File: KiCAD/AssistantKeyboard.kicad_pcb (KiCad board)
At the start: 2 copper layers, 64 x 108 mm, 14 parts, among them J1 Conn_01x04_Male, J2 Conn_01x12_Male, J3 Conn_01x12_Male, J4 Conn_01x02_Male, SW1 SW_Push, SW13 RotaryEncoder_Switch, SW2 SW_Push, SW3 SW_Push, SW4 SW_Push, SW5 SW_Push, SW6 SW_Push, SW7 SW_Push, SW8 SW_Push, SW9 SW_Push

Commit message: V1.0
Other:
- board text added: "AssistantKeyboard by A. Hensel v.1.0"
- board text removed: "AssistantKeyboard by A. Hensel v.0.9"
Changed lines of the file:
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@@
     (effects (font (size 1.5 1.5) (thickness 0.3)))
   )
-  (gr_text "AssistantKeyboard\nby A. Hensel\nv.0.9" (at 111.252 49.53) (layer "F.SilkS")
-    (effects (font (size 1 1) (thickness 0.15)))
+  (gr_text "AssistantKeyboard\nby A. Hensel\nv.1.0" (at 111.252 49.53) (layer "F.SilkS")
+    (effects (font (size 1.2 1.2) (thickness 0.15)))
   )
   (gr_text "Display I²C" (at 115.57 66.802 90) (layer "F.SilkS")

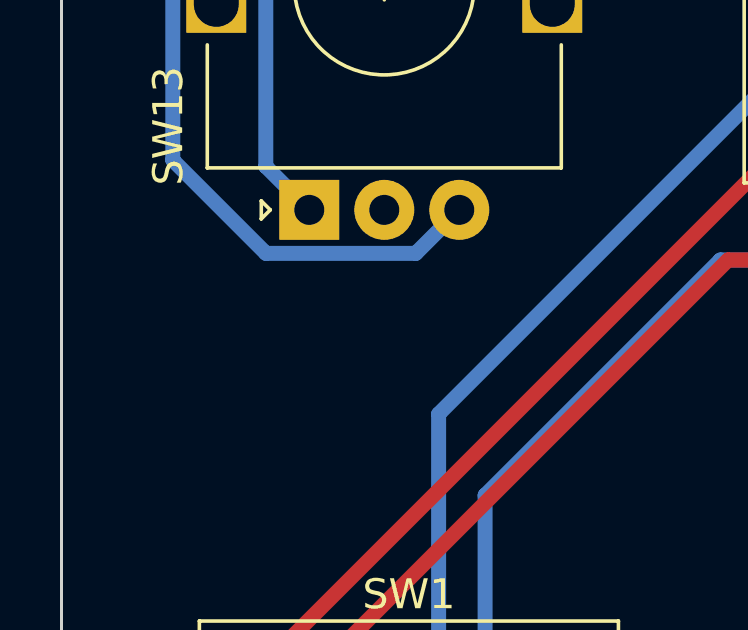
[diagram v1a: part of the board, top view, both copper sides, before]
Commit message: Debounce caps
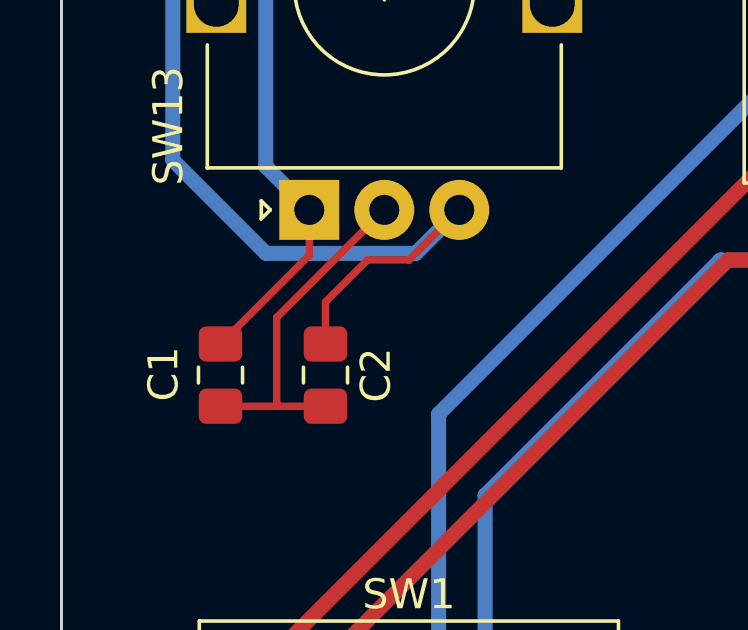
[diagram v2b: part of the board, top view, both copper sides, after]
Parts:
- added C1: 10nF, Capacitor_SMD:C_0805_2012Metric_Pad1.18x1.45mm_HandSolder, F.Cu at (62.3, 68.6)
- added C2: 10nF, Capacitor_SMD:C_0805_2012Metric_Pad1.18x1.45mm_HandSolder, F.Cu at (65.8, 68.6)
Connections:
- J2 pad 1: D9 -> unconnected-(J2-Pad1)
- J3 pad 9: D15 -> unconnected-(J3-Pad9)
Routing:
- net GND: track 0.00 -> 11.5 mm
- net D1: track 49.4 -> 56.5 mm
- net D0: track 37.1 -> 42.8 mm
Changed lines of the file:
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@@
   (net 3 "SCK")
   (net 4 "SDA")
-  (net 5 "D9")
+  (net 5 "unconnected-(J2-Pad1)")
   (net 6 "D8")
   (net 7 "D7")
@@
   (net 17 "unconnected-(J3-Pad7)")
   (net 18 "unconnected-(J3-Pad8)")
-  (net 19 "D15")
+  (net 19 "unconnected-(J3-Pad9)")
   (net 20 "D14")
   (net 21 "D16")
@@
       (net 18 "unconnected-(J3-Pad8)") (pinfunction "Pin_8") (pintype "passive+no_connect"))
     (pad "9" thru_hole oval (at 0 20.32) (size 1.7 1.7) (drill 1) (layers *.Cu *.Mask)
-      (net 19 "D15") (pinfunction "Pin_9") (pintype "passive+no_connect"))
+      (net 19 "unconnected-(J3-Pad9)") (pinfunction "Pin_9") (pintype "passive+no_connect"))
     (pad "10" thru_hole oval (at 0 22.86) (size 1.7 1.7) (drill 1) (layers *.Cu *.Mask)
       (net 20 "D14") (pinfunction "Pin_10") (pintype "passive"))
@@
     )
   )
+  (footprint "Capacitor_SMD:C_0805_2012Metric_Pad1.18x1.45mm_HandSolder" (layer "F.Cu")
+    (at 62.3 68.6375 -90)
+    (descr "Capacitor SMD 0805 (2012 Metric), square (rectangular) end terminal, IPC_7351 nominal with elongated pad for handsoldering. (Body size source: IPC-SM-782 page 76, https://www.pcb-3d.com/wordpress/wp-content/uploads/ipc-sm-782a_amendment_1_and_2.pdf, https://docs.google.com/spreadsheets/d/1BsfQQcO9C6DZCsRaXUlFlo91Tg2WpOkGARC1WS5S8t0/edit?usp=sharing), generated with kicad-footprint-generator")
+    (tags "capacitor handsolder")
+    (property "Sheetfile" "AssistantKeyboard.kicad_sch")
+    (property "Sheetname" "")
+    (attr smd)
+    (fp_text reference "C1" (at -0.0375 1.9 90) (layer "F.SilkS")
+      (effects (font (size 1 1) (thickness 0.15)))
+    )
+    (fp_text value "10nF" (at 0 1.68 90) (layer "F.Fab")
+      (effects (font (size 1 1) (thickness 0.15)))
+    )
+    (fp_text user "${REFERENCE}" (at 0 0 90) (layer "F.Fab")
+      (effects (font (size 0.5 0.5) (thickness 0.08)))
+    )
+    (fp_line (start -0.261252 0.735) (end 0.261252 0.735) (layer "F.SilkS") (width 0.12))
+    (fp_line (start -0.261252 -0.735) (end 0.261252 -0.735) (layer "F.SilkS") (width 0.12))
+    (fp_line (start 1.88 -0.98) (end 1.88 0.98) (layer "F.CrtYd") (width 0.05))
+    (fp_line (start -1.88 -0.98) (end 1.88 -0.98) (layer "F.CrtYd") (width 0.05))
+    (fp_line (start 1.88 0.98) (end -1.88 0.98) (layer "F.CrtYd") (width 0.05))
+    (fp_line (start -1.88 0.98) (end -1.88 -0.98) (layer "F.CrtYd") (width 0.05))
+    (fp_line (start -1 0.625) (end -1 -0.625) (layer "F.Fab") (width 0.1))
+    (fp_line (start -1 -0.625) (end 1 -0.625) (layer "F.Fab") (width 0.1))
+    (fp_line (start 1 0.625) (end -1 0.625) (layer "F.Fab") (width 0.1))
+    (fp_line (start 1 -0.625) (end 1 0.625) (layer "F.Fab") (width 0.1))
+    (pad "1" smd roundrect (at -1.0375 0 270) (size 1.175 1.45) (layers "F.Cu" "F.Paste" "F.Mask") (roundrect_rratio 0.212766)
+      (net 11 "D0") (pintype "passive"))
+    (pad "2" smd roundrect (at 1.0375 0 270) (size 1.175 1.45) (layers "F.Cu" "F.Paste" "F.Mask") (roundrect_rratio 0.212766)
+      (net 2 "GND") (pintype "passive"))
+    (model "${KICAD6_3DMODEL_DIR}/Capacitor_SMD.3dshapes/C_0805_2012Metric.wrl"
+      (offset (xyz 0 0 0))
+      (scale (xyz 1 1 1))
+      (rotate (xyz 0 0 0))
+    )
+  )
   (footprint "Button_Switch_Keyboard:SW_Cherry_MX_1.00u_PCB" (layer "F.Cu")
     (at 111.76 99.06)
@@
     (fp_line (start 1.27 -1.27) (end 1.27 29.21) (layer "F.Fab") (width 0.1))
     (pad "1" thru_hole rect (at 0 0 180) (size 1.7 1.7) (drill 1) (layers *.Cu *.Mask)
-      (net 5 "D9") (pinfunction "Pin_1") (pintype "passive+no_connect"))
+      (net 5 "unconnected-(J2-Pad1)") (pinfunction "Pin_1") (pintype "passive+no_connect"))
     (pad "2" thru_hole oval (at 0 2.54 180) (size 1.7 1.7) (drill 1) (layers *.Cu *.Mask)
       (net 6 "D8") (pinfunction "Pin_2") (pintype "passive"))
@@
     )
   )
+  (footprint "Capacitor_SMD:C_0805_2012Metric_Pad1.18x1.45mm_HandSolder" (layer "F.Cu")
+    (at 65.8 68.6375 -90)
+    (descr "Capacitor SMD 0805 (2012 Metric), square (rectangular) end terminal, IPC_7351 nominal with elongated pad for handsoldering. (Body size source: IPC-SM-782 page 76, https://www.pcb-3d.com/wordpress/wp-content/uploads/ipc-sm-782a_amendment_1_and_2.pdf, https://docs.google.com/spreadsheets/d/1BsfQQcO9C6DZCsRaXUlFlo91Tg2WpOkGARC1WS5S8t0/edit?usp=sharing), generated with kicad-footprint-generator")
+    (tags "capacitor handsolder")
+    (property "Sheetfile" "AssistantKeyboard.kicad_sch")
+    (property "Sheetname" "")
+    (attr smd)
+    (fp_text reference "C2" (at 0 -1.68 90) (layer "F.SilkS")
+      (effects (font (size 1 1) (thickness 0.15)))
+    )
+    (fp_text value "10nF" (at 0 1.68 90) (layer "F.Fab")
+      (effects (font (size 1 1) (thickness 0.15)))
+    )
+    (fp_text user "${REFERENCE}" (at 0 0 90) (layer "F.Fab")
+      (effects (font (size 0.5 0.5) (thickness 0.08)))
+    )
+    (fp_line (start -0.261252 0.735) (end 0.261252 0.735) (layer "F.SilkS") (width 0.12))
+    (fp_line (start -0.261252 -0.735) (end 0.261252 -0.735) (layer "F.SilkS") (width 0.12))
+    (fp_line (start -1.88 0.98) (end -1.88 -0.98) (layer "F.CrtYd") (width 0.05))
+    (fp_line (start -1.88 -0.98) (end 1.88 -0.98) (layer "F.CrtYd") (width 0.05))
+    (fp_line (start 1.88 0.98) (end -1.88 0.98) (layer "F.CrtYd") (width 0.05))
+    (fp_line (start 1.88 -0.98) (end 1.88 0.98) (layer "F.CrtYd") (width 0.05))
+    (fp_line (start -1 0.625) (end -1 -0.625) (layer "F.Fab") (width 0.1))
+    (fp_line (start 1 -0.625) (end 1 0.625) (layer "F.Fab") (width 0.1))
+    (fp_line (start -1 -0.625) (end 1 -0.625) (layer "F.Fab") (width 0.1))
+    (fp_line (start 1 0.625) (end -1 0.625) (layer "F.Fab") (width 0.1))
+    (pad "1" smd roundrect (at -1.0375 0 270) (size 1.175 1.45) (layers "F.Cu" "F.Paste" "F.Mask") (roundrect_rratio 0.212766)
+      (net 12 "D1") (pintype "passive"))
+    (pad "2" smd roundrect (at 1.0375 0 270) (size 1.175 1.45) (layers "F.Cu" "F.Paste" "F.Mask") (roundrect_rratio 0.212766)
+      (net 2 "GND") (pintype "passive"))
+    (model "${KICAD6_3DMODEL_DIR}/Capacitor_SMD.3dshapes/C_0805_2012Metric.wrl"
+      (offset (xyz 0 0 0))
+      (scale (xyz 1 1 1))
+      (rotate (xyz 0 0 0))
+    )
+  )
   (gr_rect (start 83.82 35.052) (end 118.11 70.612) (layer "Dwgs.User") (width 0.15) (fill none))
   (gr_rect (start 79.546 31.65) (end 97.746 65.15) (layer "Dwgs.User") (width 0.15) (fill none))
@@
     (effects (font (size 1.5 1.5) (thickness 0.3)))
   )
+  (segment (start 64.175 66.714466) (end 67.759466 63.13) (width 0.25) (layer "F.Cu") (net 2))
+  (segment (start 62.3 69.675) (end 64.175 69.675) (width 0.25) (layer "F.Cu") (net 2))
+  (segment (start 64.175 69.675) (end 65.8 69.675) (width 0.25) (layer "F.Cu") (net 2))
+  (segment (start 64.175 69.675) (end 64.175 66.714466) (width 0.25) (layer "F.Cu") (net 2))
   (segment (start 109.22 71.12) (end 100.400489 62.300489) (width 0.3) (layer "F.Cu") (net 3))
   (segment (start 95.829145 62.300489) (end 94.883634 63.246) (width 0.3) (layer "F.Cu") (net 3))
@@
   (segment (start 65.259466 48.63) (end 67.429466 50.8) (width 0.5) (layer "B.Cu") (net 10))
   (segment (start 67.429466 50.8) (end 81.086 50.8) (width 0.5) (layer "B.Cu") (net 10))
+  (segment (start 65.259466 64.640534) (end 65.259466 63.13) (width 0.25) (layer "F.Cu") (net 11))
+  (segment (start 62.3 67.6) (end 65.259466 64.640534) (width 0.25) (layer "F.Cu") (net 11))
   (segment (start 63.809955 48.029592) (end 73.739547 38.1) (width 0.5) (layer "B.Cu") (net 11))
   (segment (start 73.739547 38.1) (end 81.086 38.1) (width 0.5) (layer "B.Cu") (net 11))
   (segment (start 65.259466 63.13) (end 63.809955 61.680489) (width 0.5) (layer "B.Cu") (net 11))
   (segment (start 63.809955 61.680489) (end 63.809955 48.029592) (width 0.5) (layer "B.Cu") (net 11))
+  (segment (start 65.8 66.2) (end 67.2 64.8) (width 0.25) (layer "F.Cu") (net 12))
+  (segment (start 67.2 64.8) (end 68.589466 64.8) (width 0.25) (layer "F.Cu") (net 12))
+  (segment (start 68.589466 64.8) (end 70.259466 63.13) (width 0.25) (layer "F.Cu") (net 12))
+  (segment (start 65.8 67.6) (end 65.8 66.2) (width 0.25) (layer "F.Cu") (net 12))
   (segment (start 74.93 35.56) (end 81.086 35.56) (width 0.5) (layer "B.Cu") (net 12))
   (segment (start 60.709955 49.780045) (end 74.93 35.56) (width 0.5) (layer "B.Cu") (net 12))

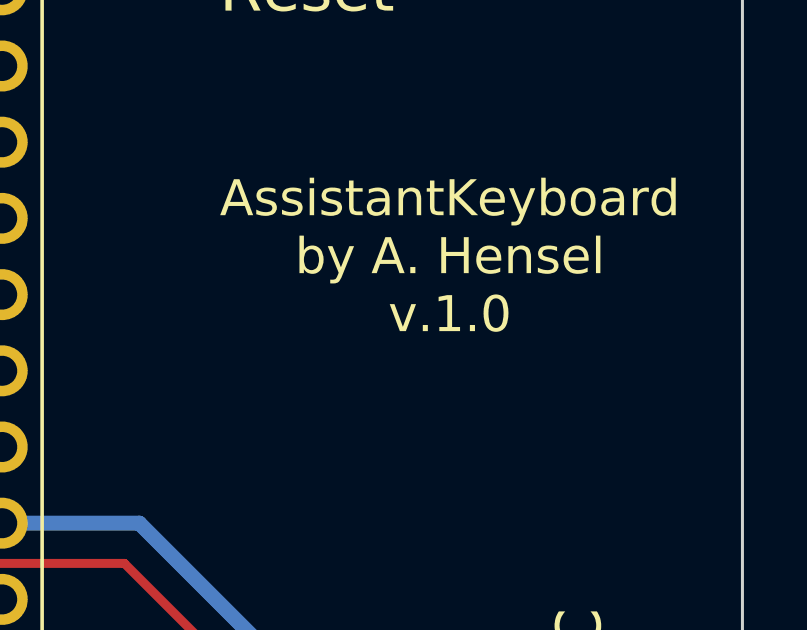
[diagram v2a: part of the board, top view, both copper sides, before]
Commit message: Documentation, version number on pcb silk screen
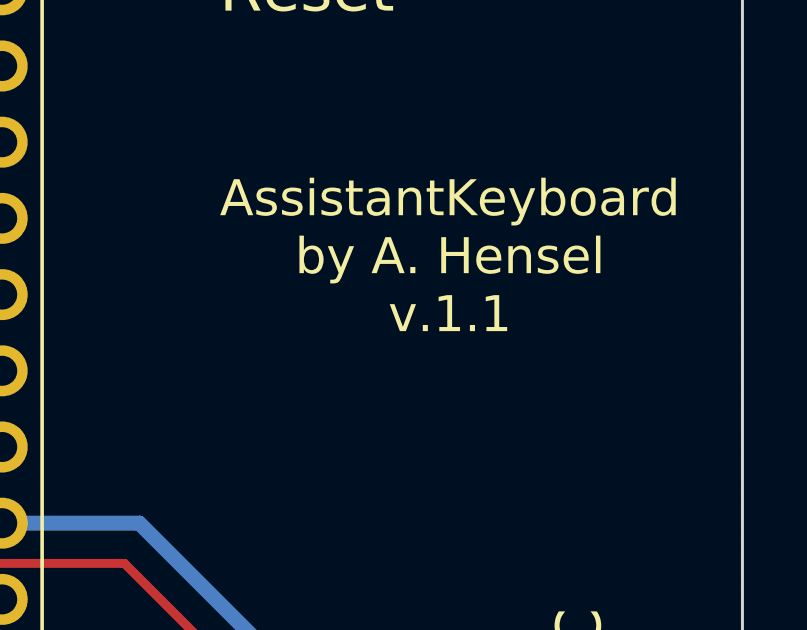
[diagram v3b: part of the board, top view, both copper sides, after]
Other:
- board text added: "AssistantKeyboard by A. Hensel v.1.1"
- board text removed: "AssistantKeyboard by A. Hensel v.1.0"
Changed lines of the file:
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@@
   )
   (paper "A4")
-  (title_block
-    (comment 4 "AISLER Project ID: SNZYUZXY")
-  )
   (layers
     (0 "F.Cu" signal)
@@
     (effects (font (size 1.5 1.5) (thickness 0.3)))
   )
-  (gr_text "AssistantKeyboard\nby A. Hensel\nv.1.0" (at 111.252 49.53) (layer "F.SilkS")
+  (gr_text "AssistantKeyboard\nby A. Hensel\nv.1.1" (at 111.252 49.53) (layer "F.SilkS")
     (effects (font (size 1.2 1.2) (thickness 0.15)))
   )
